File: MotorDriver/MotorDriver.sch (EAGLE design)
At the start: 78 parts, among them IC1 DRV8320RSRHAR, IC2 MAX3051ESA+, J1 J_USB_MICROAB_HIROSE_ZX62-AB-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, J2 SM03B-ZESS-TB, Q1 BUK7Y7R8-80EX, Q2 BUK7Y7R8-80EX, Q3 BUK7Y7R8-80EX, Q4 BUK7Y7R8-80EX, Q5 BUK7Y7R8-80EX, Q6 BUK7Y7R8-80EX, U1 LPC1549JBD48, U3 MCP1700T-33, U4 ADR5041, Y1 FA238V

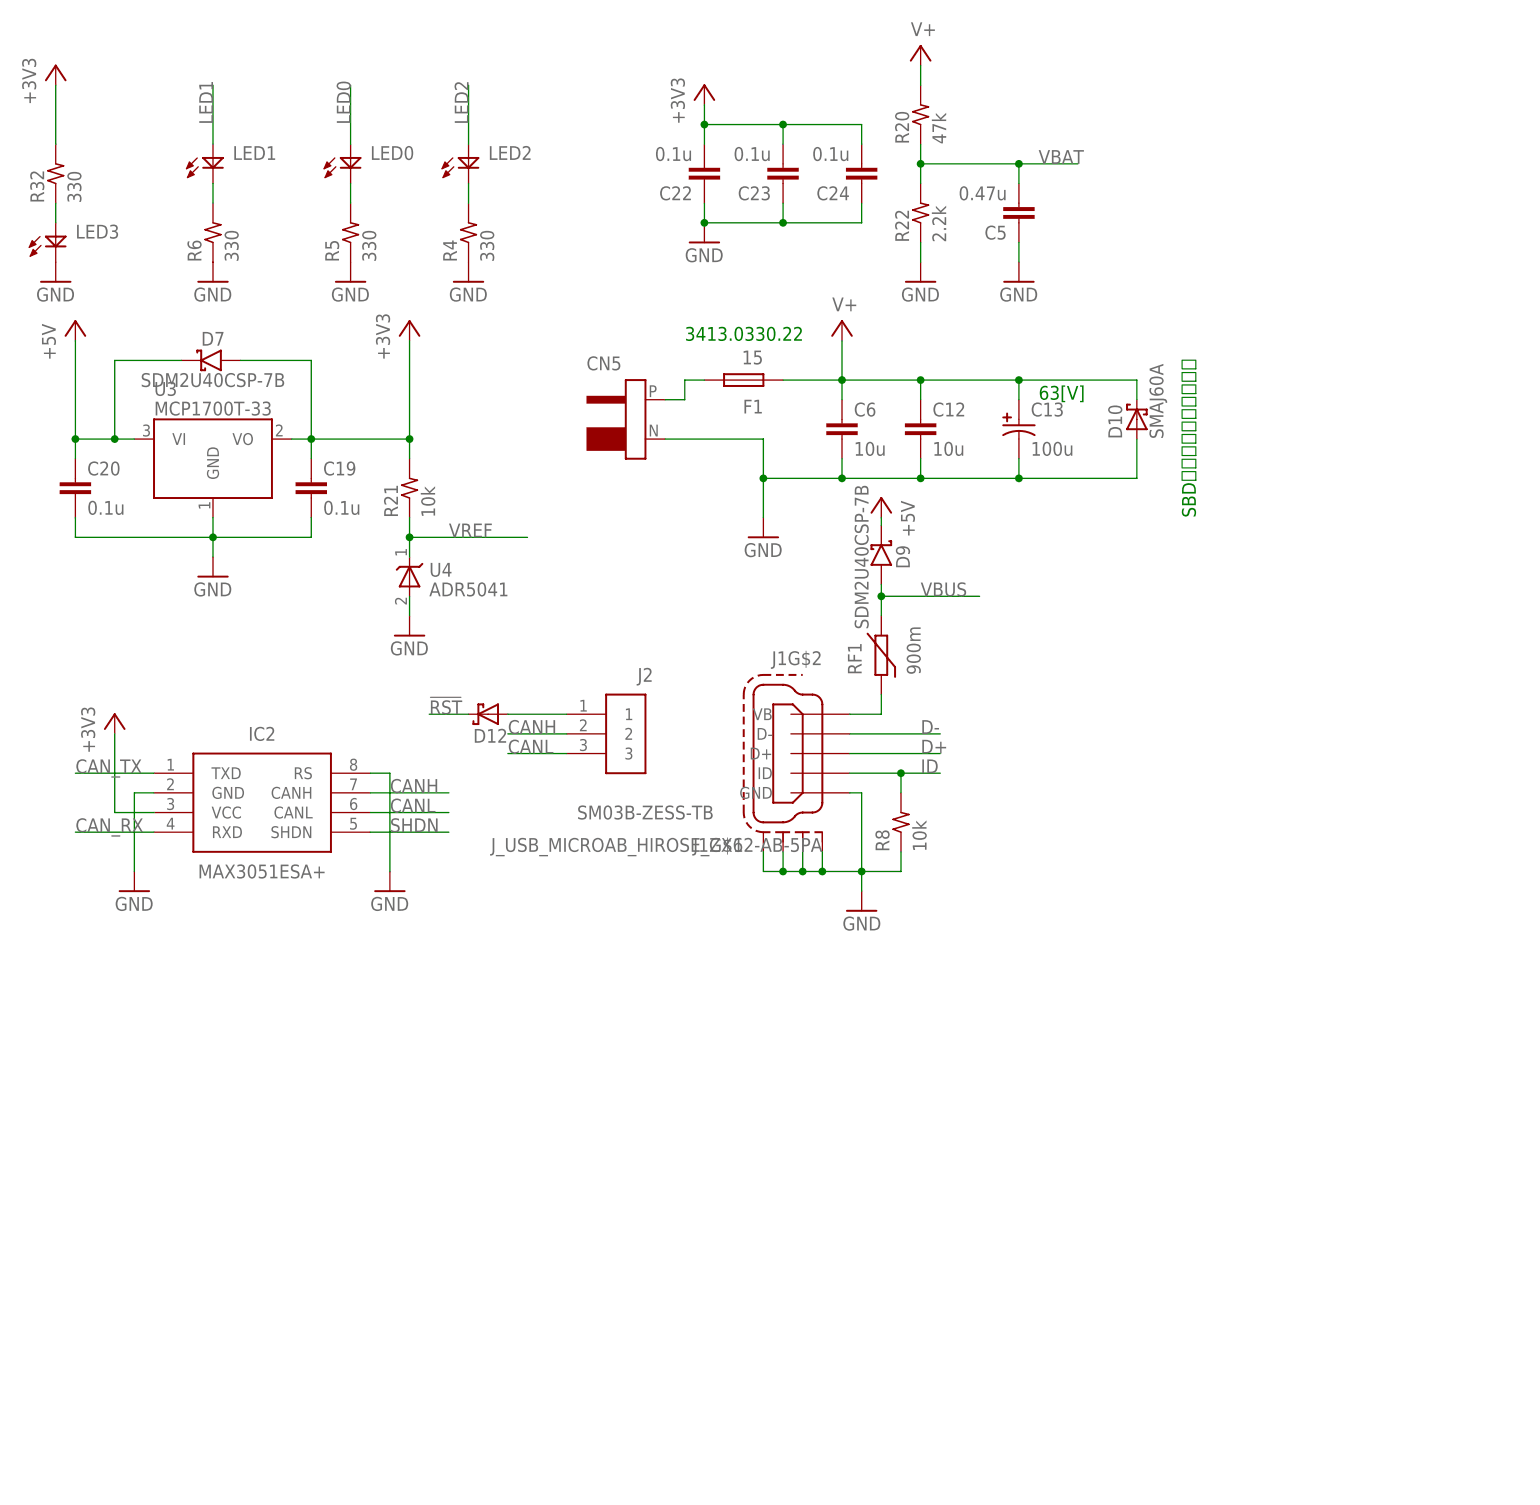
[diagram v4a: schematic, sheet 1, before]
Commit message: ヒューズ切断検出機能を追加
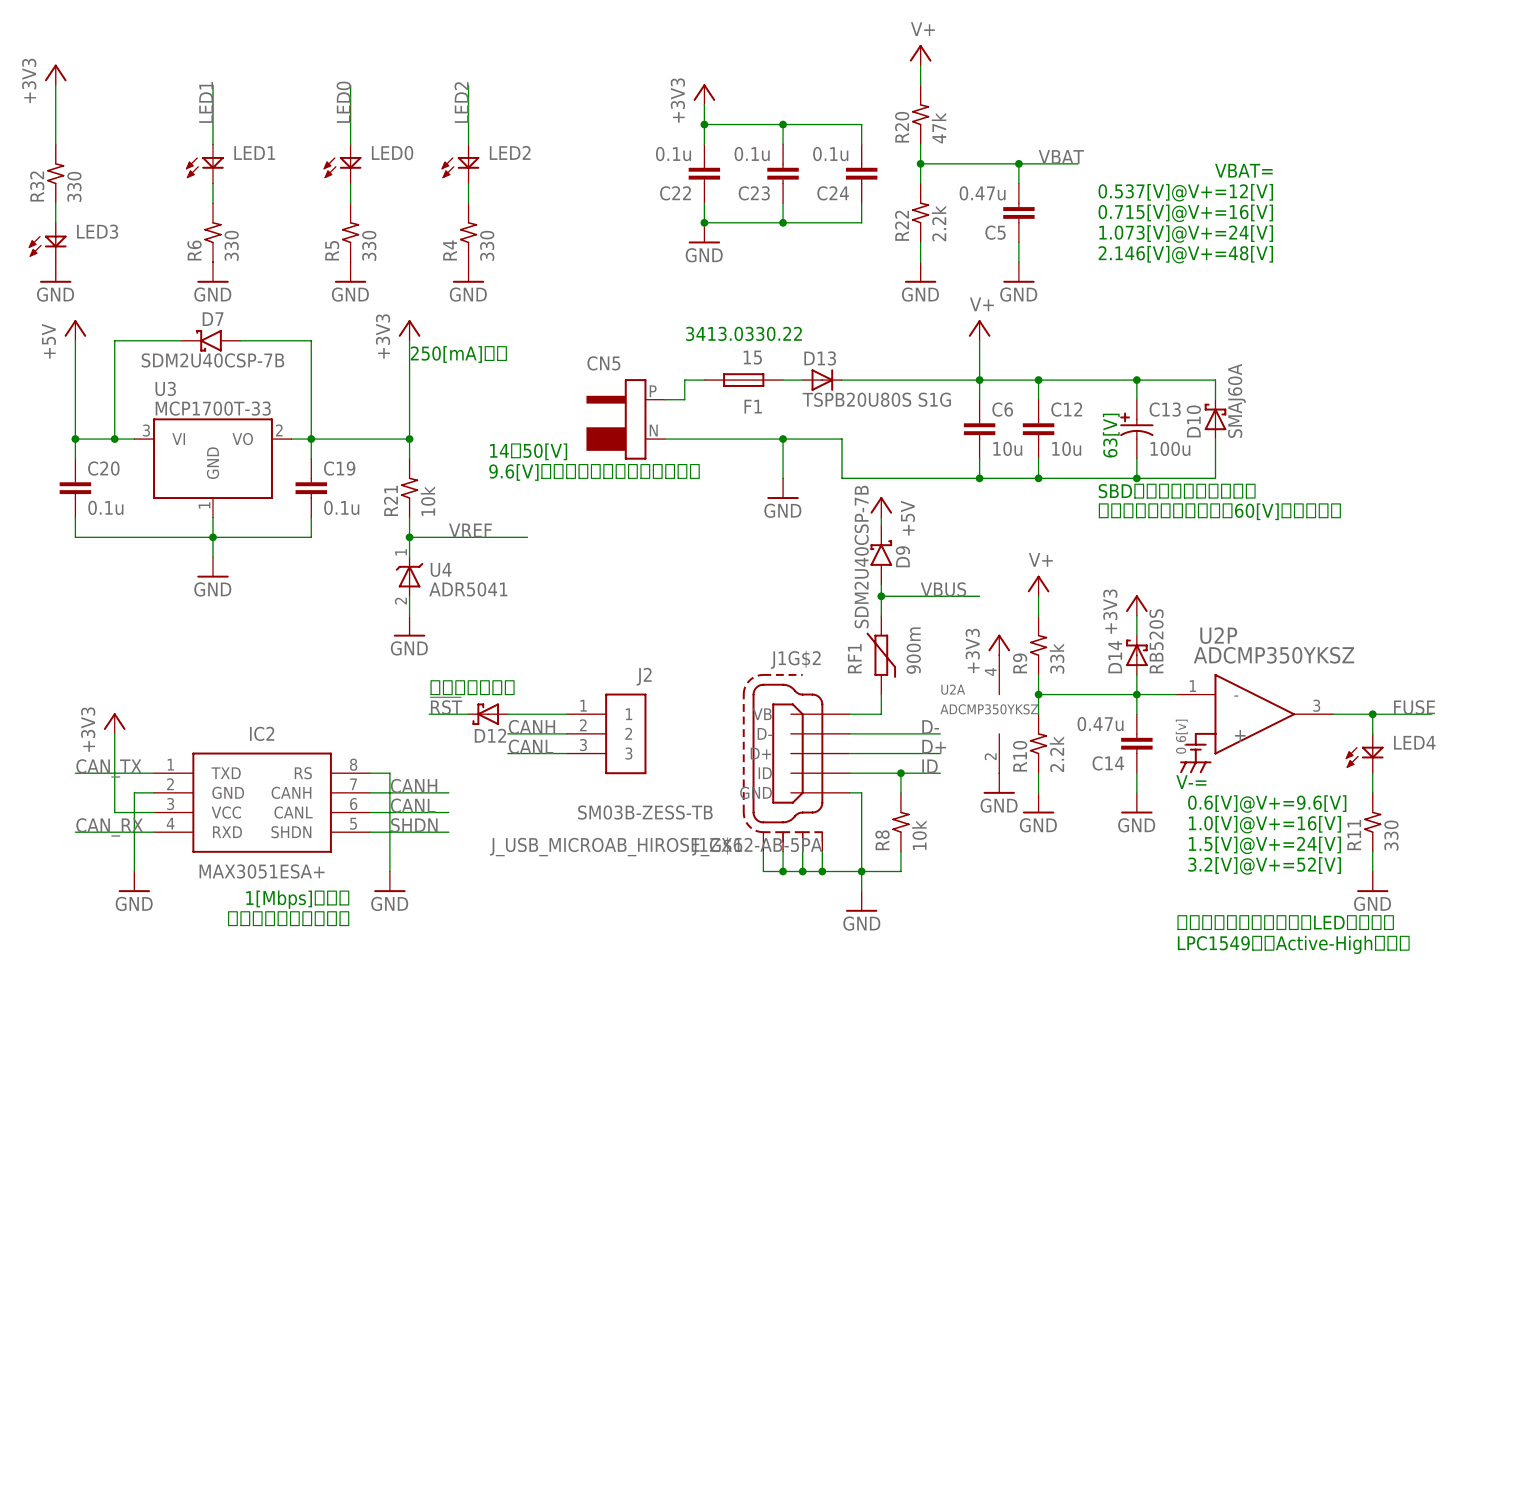
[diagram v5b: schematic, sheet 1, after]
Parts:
- added C14: 0.47u, MotorDriver:C1005
- added D13: TSPB20U80S S1G, Diode:DIODE-SMPC
- added D14: RB520S, MotorDriver:SBD-SOD523
- added LED4: (no value), MotorDriver:LED1608
- added R10: 2.2k, MotorDriver:R1608
- added R11: 330, MotorDriver:R1005
- added R9: 33k, MotorDriver:R1608
- added U2: ADCMP350YKSZ, adcmp350:ADCMP350YKSZ
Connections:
- new net FUSE: LED4.A, U1.SWDIO/PIO0_20/SCT1_OUT6/TMS, U2P.OUT
- new net N$25: C14.2, D14.A, R10.2, R9.1, U2P.-
- new net N$27: LED4.K, R11.2
- net +3V3: now also D14.K, U1.VBAT, U1.VDD(1), U2A.VCC
- net GND: now also C14.1, R10.1, R11.1, U2A.GND
- net N$23: now also D13.A, F1.1; no longer U1.VBAT, U1.VDD(1)
- net V+: now also D13.K, R9.2; no longer F1.1
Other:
- note added: "14～50[V] 9.6[V]以下はヒューズ切断と誤検知"
- note added: "1PWMモードで動作させる DCモータ用にLPCとも結合"
- note added: "1[Mbps]で動作 スルーレート制御なし"
- note added: "250[mA]まで"
- note added: "DFUはUSBしか使わないと仮定"
- note added: "V-= 0.6[V]@V+=9.6[V] 1.0[V]@V+=16[V] 1.5[V]@V+=24[V] 3.2[V]@V+=52[V]"
- note added: "VBAT= 0.537[V]@V+=12[V] 0.715[V]@V+=16[V] 1.073[V]@V+=24[V] 2.146[V]@V+=48[V]"
- note added: "ヒューズが切れていたらLEDが切れる LPC1549のｍActive-Highで入力"
- note added: "単方向リセット"
- note added: "電源端子間はツェナーで60[V]までに制限"
- moved on the sheet: C10, C11, C12, C13, C6, D10, D7, L1, Y1A

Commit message: USBラインの保護を強化した
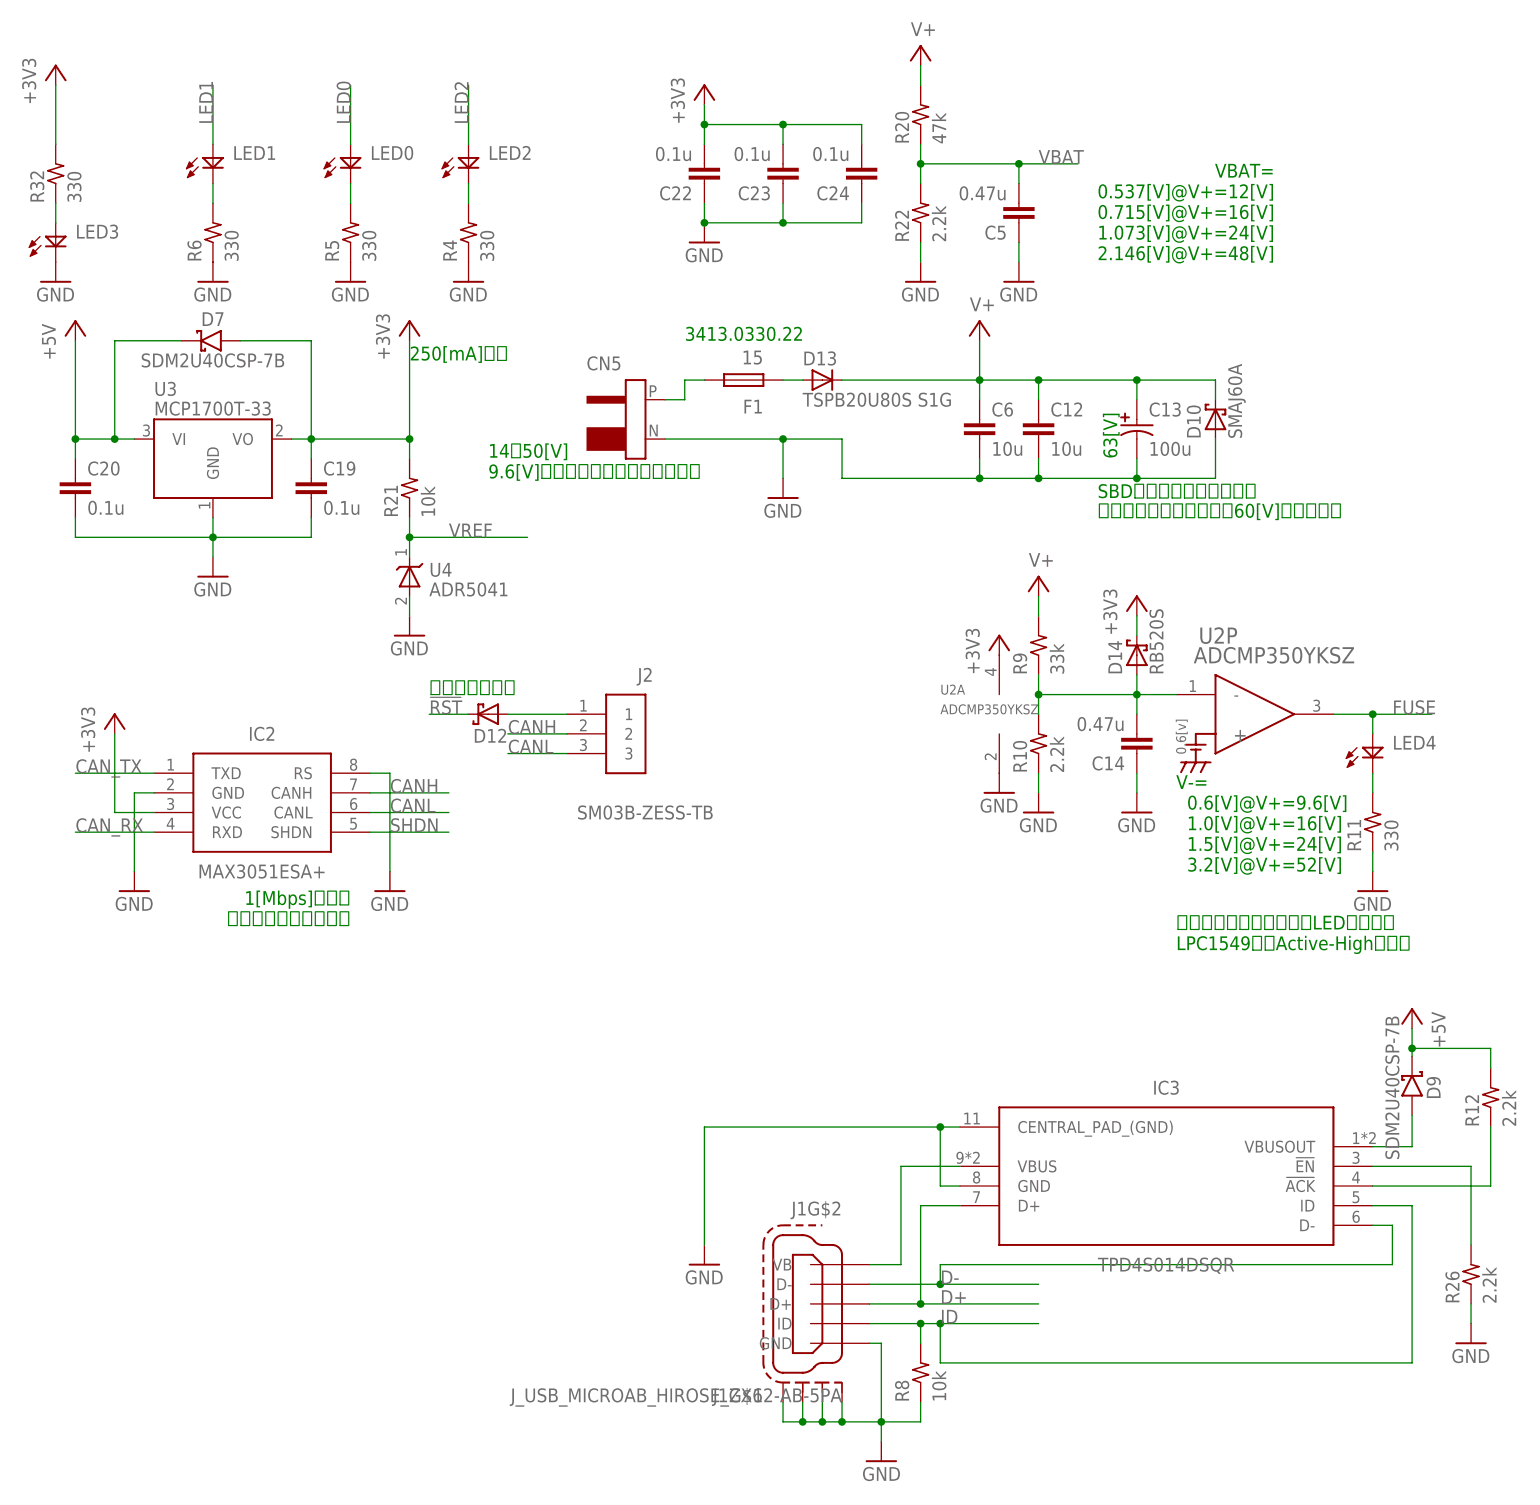
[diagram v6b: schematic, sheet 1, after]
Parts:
- removed RF1: 900m, Passive:RF1608
- added IC3: TPD4S014DSQR, TPD4S014DSQR:TPD4S014DSQR
- added R12, R26: 2.2k, MotorDriver:R1005
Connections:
- new net N$28: IC3.!EN, R26.2
- new net N$29: IC3.!ACK, R12.1
- net +5V: now also R12.2
- net D+: now also IC3.D+
- net D-: now also IC3.D-
- net GND: now also IC3.CENTRAL_PAD_(GND), IC3.GND, R26.1
- net ID: now also IC3.ID
- net N$14: now also IC3.VBUS; no longer RF1.1
- net VBUS: now also IC3.VBUSOUT; no longer RF1.2, U1.PIO0_13/ADC1_6
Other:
- moved on the sheet: D9, J1G$1, J1G$2, R8

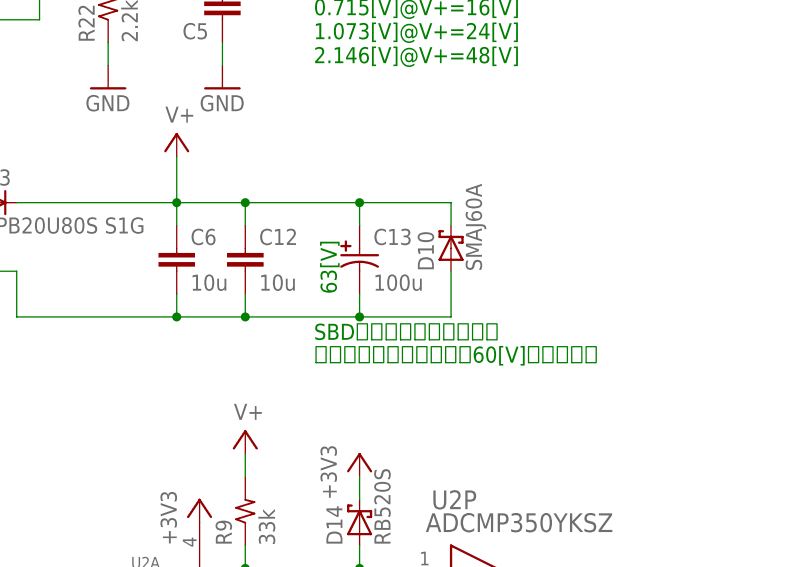
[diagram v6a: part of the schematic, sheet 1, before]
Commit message: [fix]電源補助コンデンサの容量を小さくした
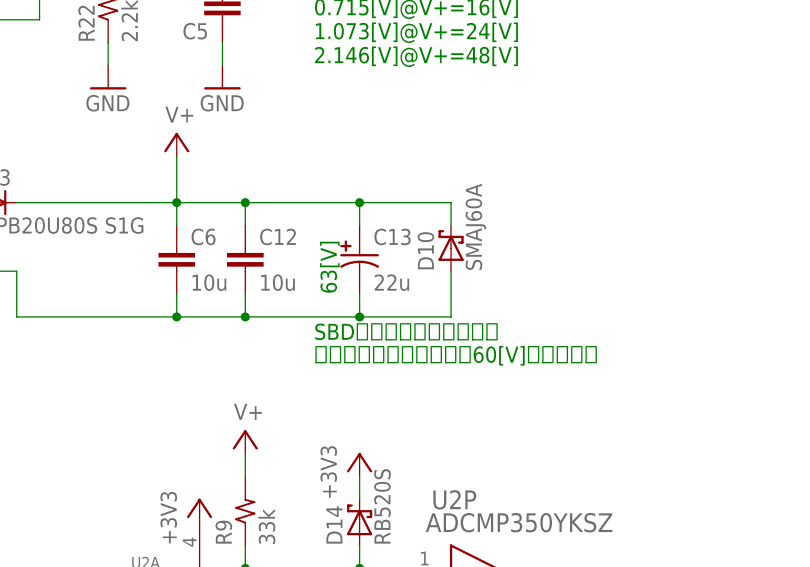
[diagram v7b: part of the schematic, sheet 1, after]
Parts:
- C13: value 100u -> 22u; device Passive:CPOLS-10 -> Passive:CPOLS-6.3
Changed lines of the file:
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@@
 <?xml version="1.0" encoding="utf-8"?>
 <!DOCTYPE eagle SYSTEM "eagle.dtd">
-<eagle version="8.4.1">
+<eagle version="8.4.3">
 <drawing>
 <settings>
@@
 <part name="GND20" library="supply1" deviceset="GND" device=""/>
 <part name="F1" library="Passive" library_urn="urn:adsk.eagle:library:1073310" deviceset="F" device="3216" package3d_urn="urn:adsk.eagle:package:1073356/2" value="15"/>
-<part name="C13" library="Passive" library_urn="urn:adsk.eagle:library:1073310" deviceset="CPOL" device="S-10" package3d_urn="urn:adsk.eagle:package:1073378/1" value="100u"/>
+<part name="C13" library="Passive" library_urn="urn:adsk.eagle:library:1073310" deviceset="CPOL" device="S-6.3" package3d_urn="urn:adsk.eagle:package:1073376/1" value="22u"/>
 <part name="R8" library="MotorDriver" library_urn="urn:adsk.eagle:library:1073580" deviceset="R" device="1005" package3d_urn="urn:adsk.eagle:package:1073655/2" value="10k"/>
 <part name="D13" library="Diode" deviceset="DIODE-*" device="SMPC" value="TSPB20U80S S1G"/>
